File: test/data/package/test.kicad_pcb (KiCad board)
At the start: 2 copper layers, 100.7 x 80 mm, 68 parts, among them P1 CONN_2, P2 CONN_2, P3 CONN_2, P4 CONN_2, P5 CONN_2, P6 CONN_2, Q1 MPSA92, Q2 MPSA42, Q3 MPSA92, Q4 MPSA42, Q5 MPSA92, Q6 MPSA42, Q7 MPSA92, Q8 MPSA42, U1 ICL7660, U2 78L05, U3 LM358N, U4 LM358N

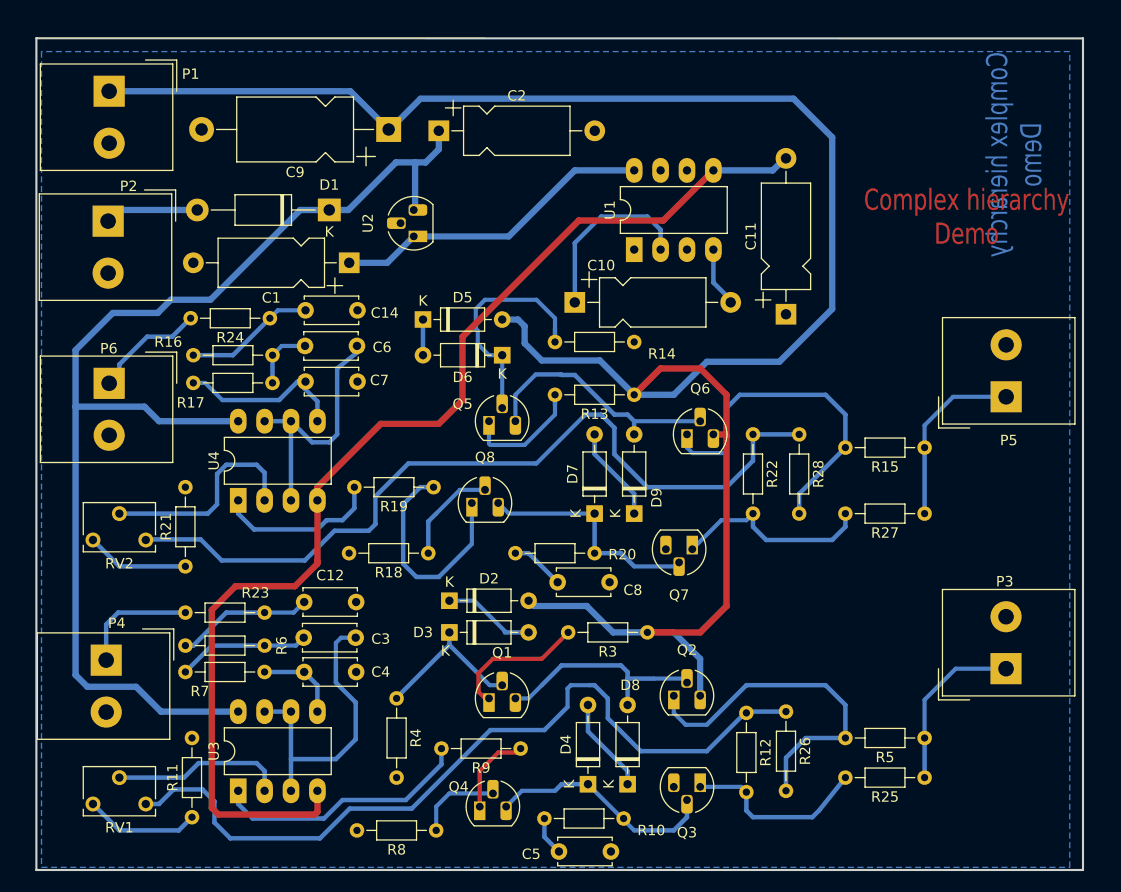
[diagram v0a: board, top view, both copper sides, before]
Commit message: impl: add reset in iter; update: alias and test case
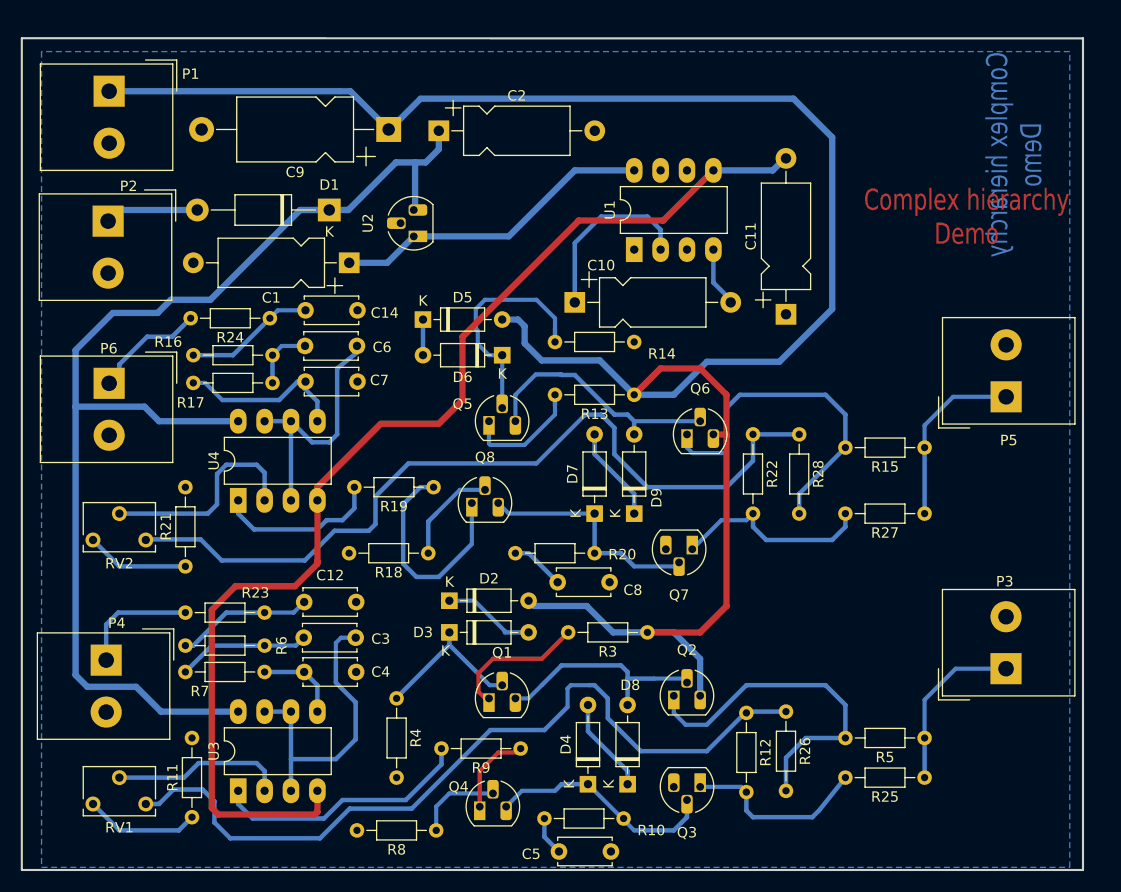
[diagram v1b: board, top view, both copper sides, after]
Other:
- board size 100.7 x 80 mm -> 102.1 x 80 mm
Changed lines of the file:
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@@
 	)
 	(gr_line
-		(start 87.9 131.826)
-		(end 87.9 51.8)
+		(start 86.5 131.826)
+		(end 86.5 51.8)
 		(stroke
 			(width 0.2032)
@@
 	(gr_line
 		(start 188.595 131.826)
-		(end 87.9 131.826)
+		(end 86.5 131.826)
 		(stroke
 			(width 0.2032)
@@
 	)
 	(gr_line
-		(start 87.9 51.8)
+		(start 86.5 51.8)
 		(end 188.595 51.816)
 		(stroke
